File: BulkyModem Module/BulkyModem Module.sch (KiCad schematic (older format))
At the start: 13 parts, among them M1 Mounting, M2 Mounting, M3 Mounting, M4 Mounting, U1 74HCT244, U6 74HCT32

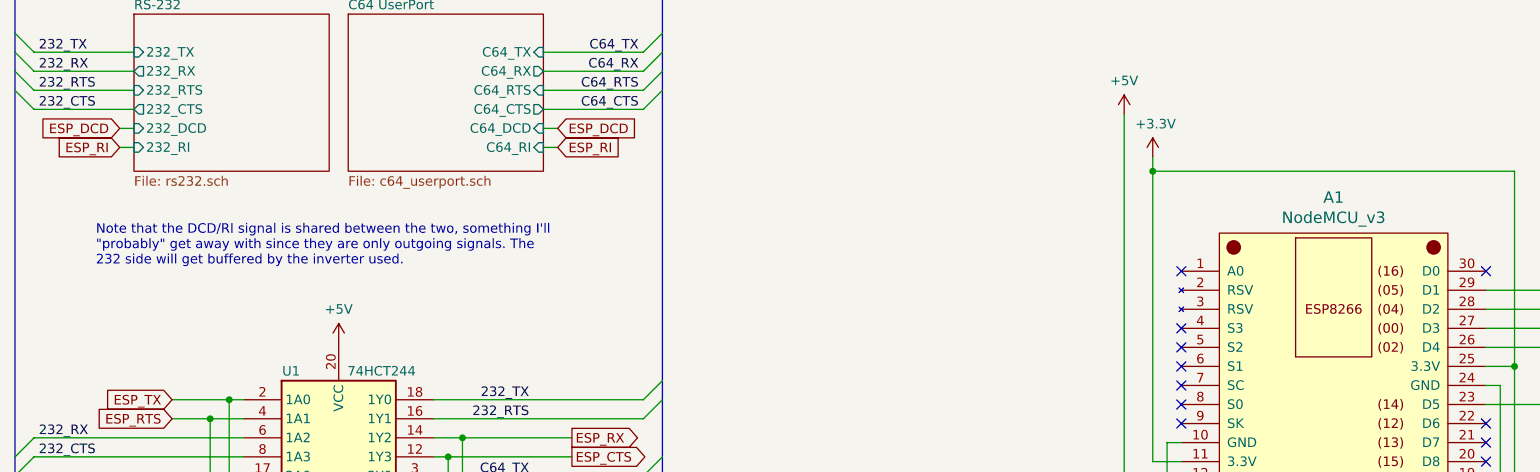
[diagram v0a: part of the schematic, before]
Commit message: Updated UserPort layout
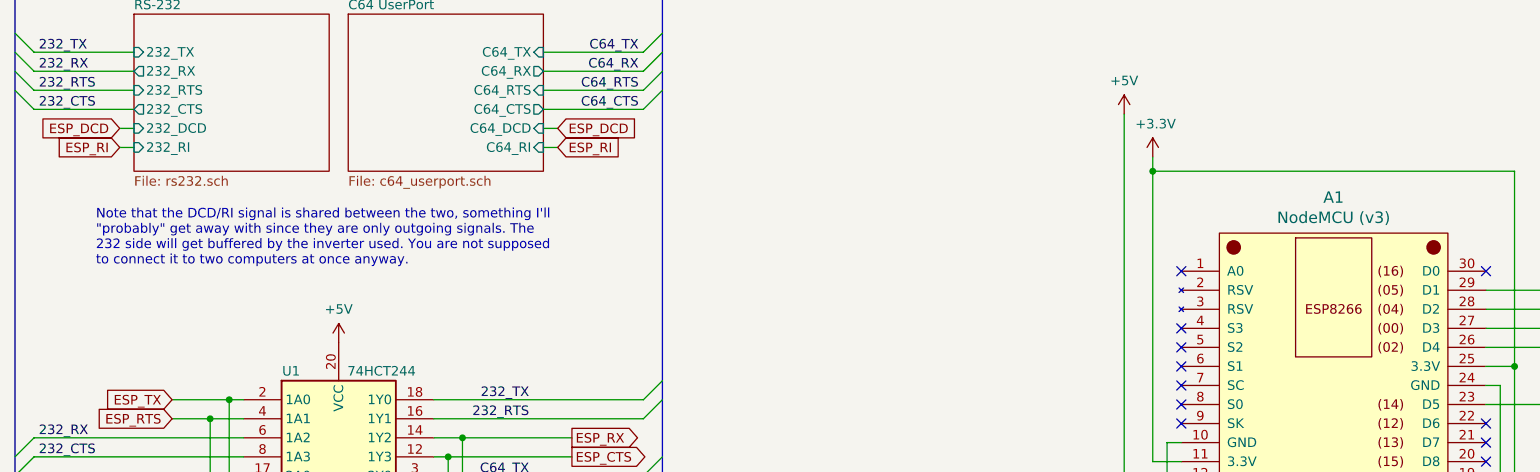
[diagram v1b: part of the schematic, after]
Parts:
- A1: value NodeMCU_v3 -> NodeMCU (v3)
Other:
- note added: "Note that the DCD/RI signal is shared between the two, something I'll\n"probably" get away with since they are only outgoing signals. The\n232 side will get buffered by the inverter used. You are not supposed\nto connect it to two computers at once anyway."
- note removed: "Note that the DCD/RI signal is shared between the two, something I'll\n"probably" get away with since they are only outgoing signals. The\n232 side will get buffered by the inverter used."
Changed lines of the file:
@@
 P 7650 3625
 F 0 "A1" H 7650 4712 60  0000 C CNN
-F 1 "NodeMCU_v3" H 7650 4606 60  0000 C CNN
+F 1 "NodeMCU (v3)" H 7650 4606 60  0000 C CNN
 F 2 "nodemcu_v3:NodeMCU-LoLinV3" H 7050 2775 60  0001 C CNN
 F 3 "" H 7050 2775 60  0000 C CNN
@@
 	3575 2175 3500 2175
 Text Notes 1150 2900 0    50   ~ 0
-Note that the DCD/RI signal is shared between the two, something I'll\n"probably" get away with since they are only outgoing signals. The\n232 side will get buffered by the inverter used.
+Note that the DCD/RI signal is shared between the two, something I'll\n"probably" get away with since they are only outgoing signals. The\n232 side will get buffered by the inverter used. You are not supposed\nto connect it to two computers at once anyway.
 Text GLabel 1275 2275 0    50   Input ~ 0
 ESP_RI

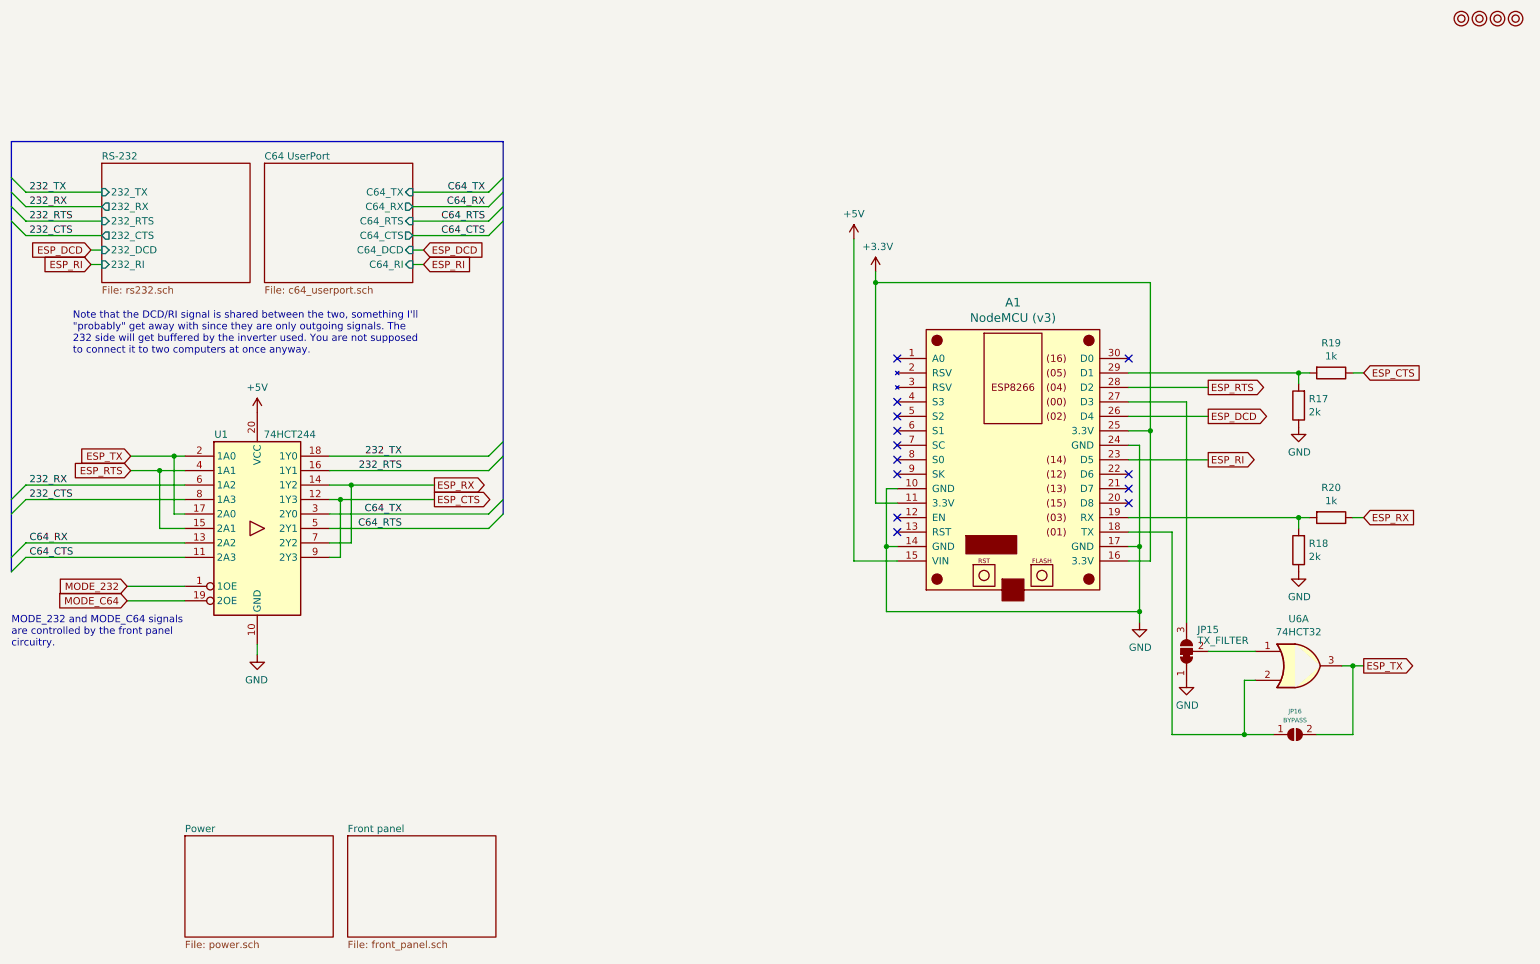
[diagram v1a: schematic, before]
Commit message: Revised version. Mainly buffering signals
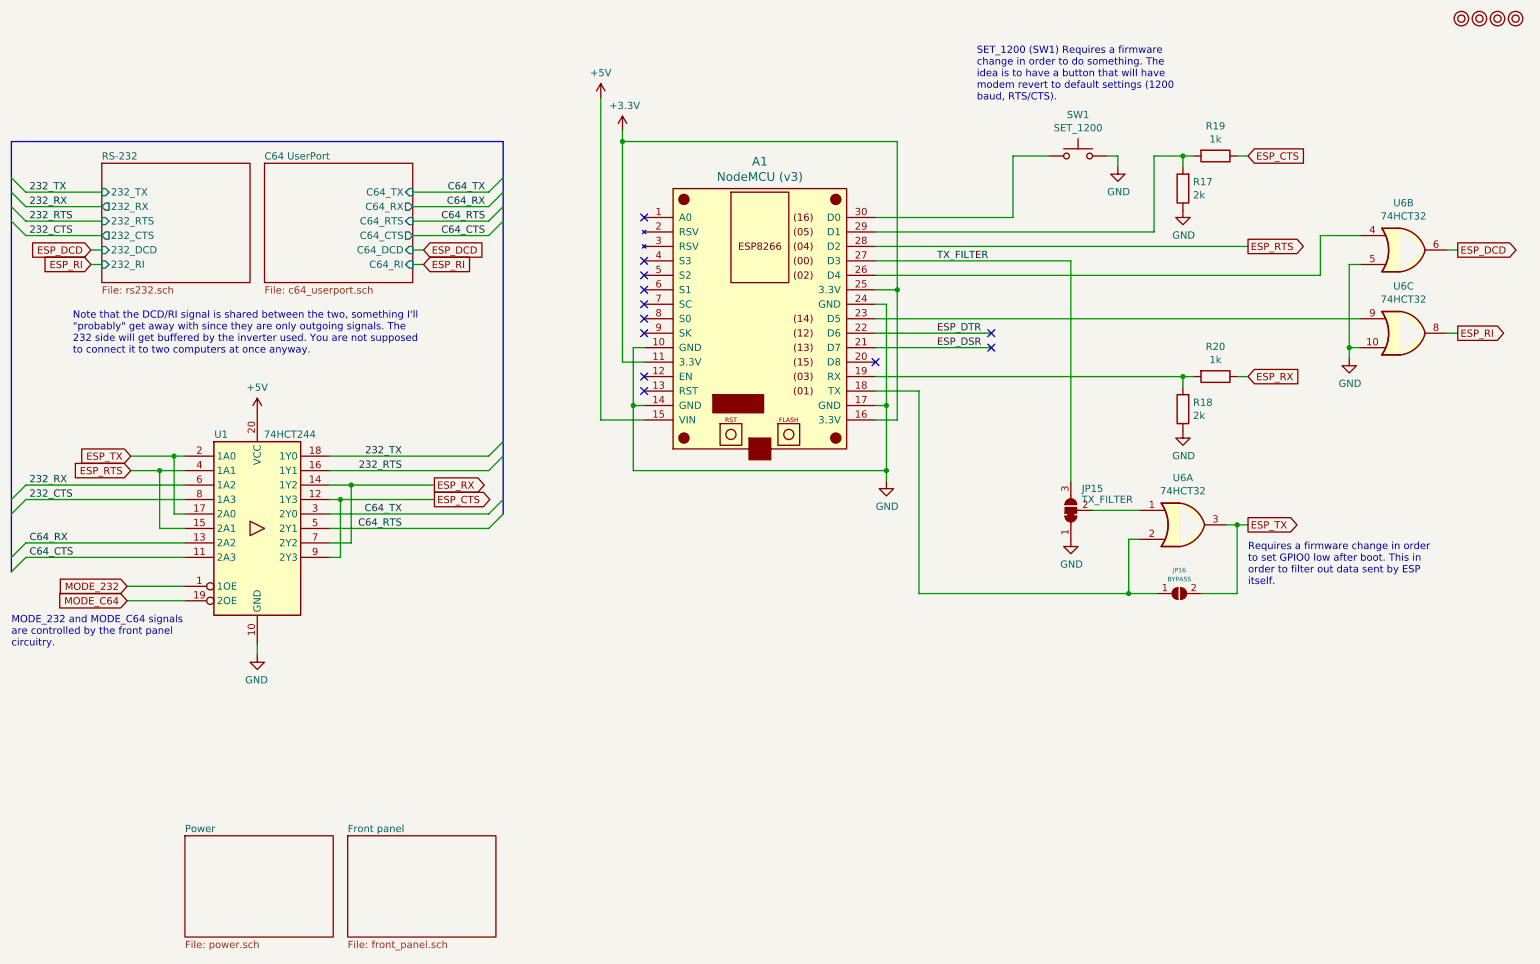
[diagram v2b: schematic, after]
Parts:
- added SW1: SET_1200, Button_Switch_THT:SW_Tactile_SPST_Angled_PTS645Vx39-2LFS, symbol Switch:SW_Push
- added unit 2 of U6
- added unit 3 of U6
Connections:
- net ESP_DCD: now also U6.6; no longer A1.26 (D4)
- net ESP_RI: now also U6.8; no longer A1.23 (D5)
- net GND: now also SW1.2, U6.10, U6.5
- net ESP_DSR: now reaches A1.21 (D7)
- net ESP_DTR: now reaches A1.22 (D6)
- net TX_FILTER: now reaches A1.27 (D3), JP15.3 (B)
- net at A1.30 (D0): now also SW1.1
- new net: A1.23 (D5), U6.9
- new net: A1.26 (D4), U6.4
- no-connect marks 13 -> 12
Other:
- note added: "Requires a firmware change in order\nto set GPIO0 low after boot. This in\norder to filter out data sent by ESP\nitself."
- note added: "SET_1200 (SW1) Requires a firmware\nchange in order to do something. The\nidea is to have a button that will have\nmodem revert to default settings (1200\nbaud, RTS/CTS)."
- moved on the sheet: A1, JP15, JP16, R17, R18, R19, R20, U6A

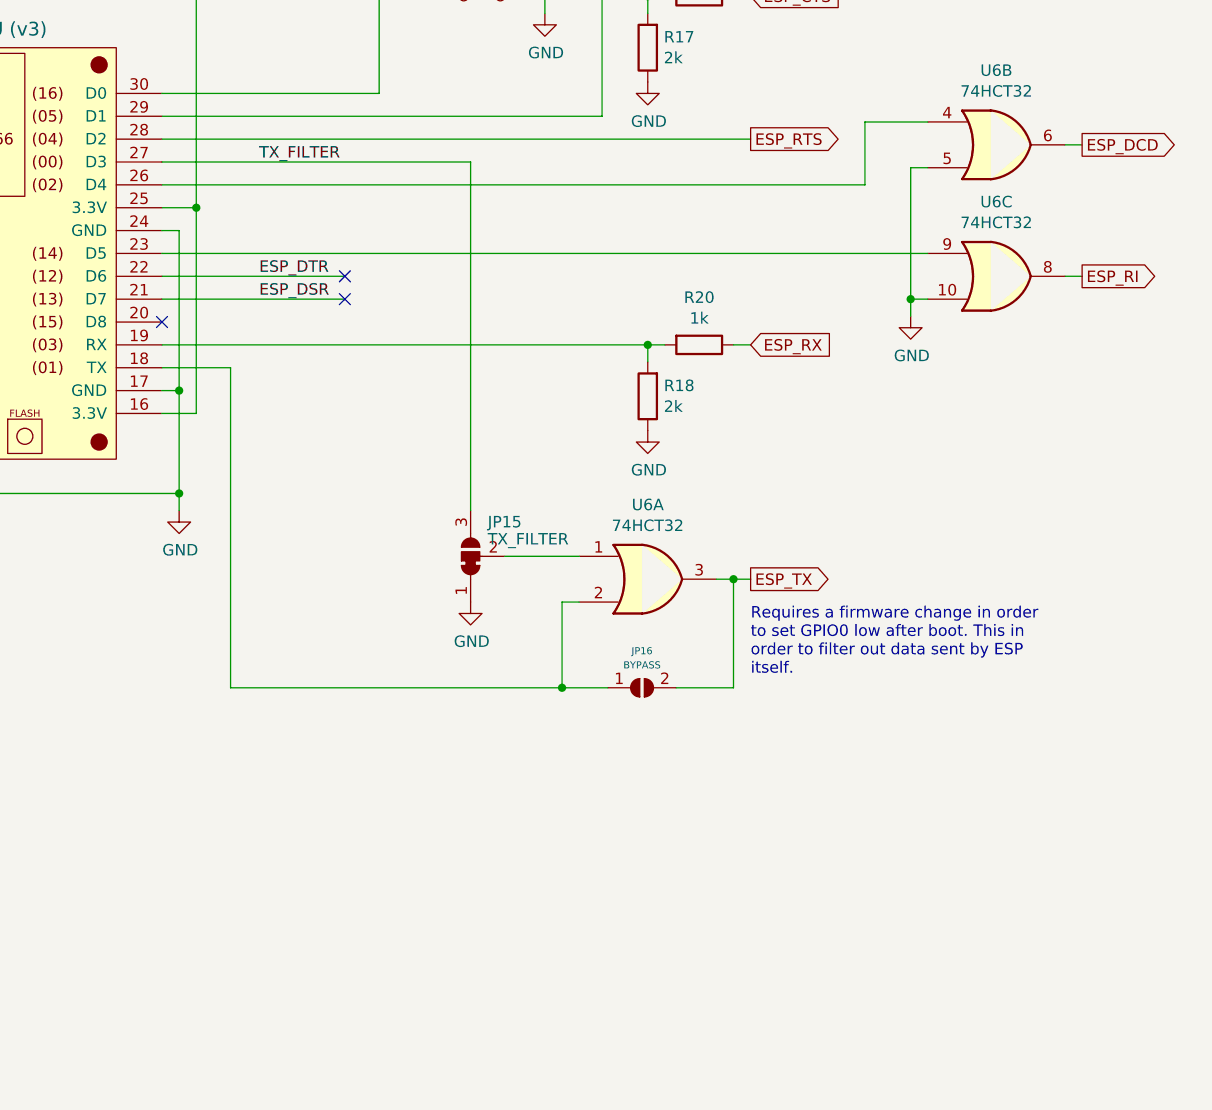
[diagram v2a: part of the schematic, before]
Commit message: Tweaks needed to make revision C actually work.
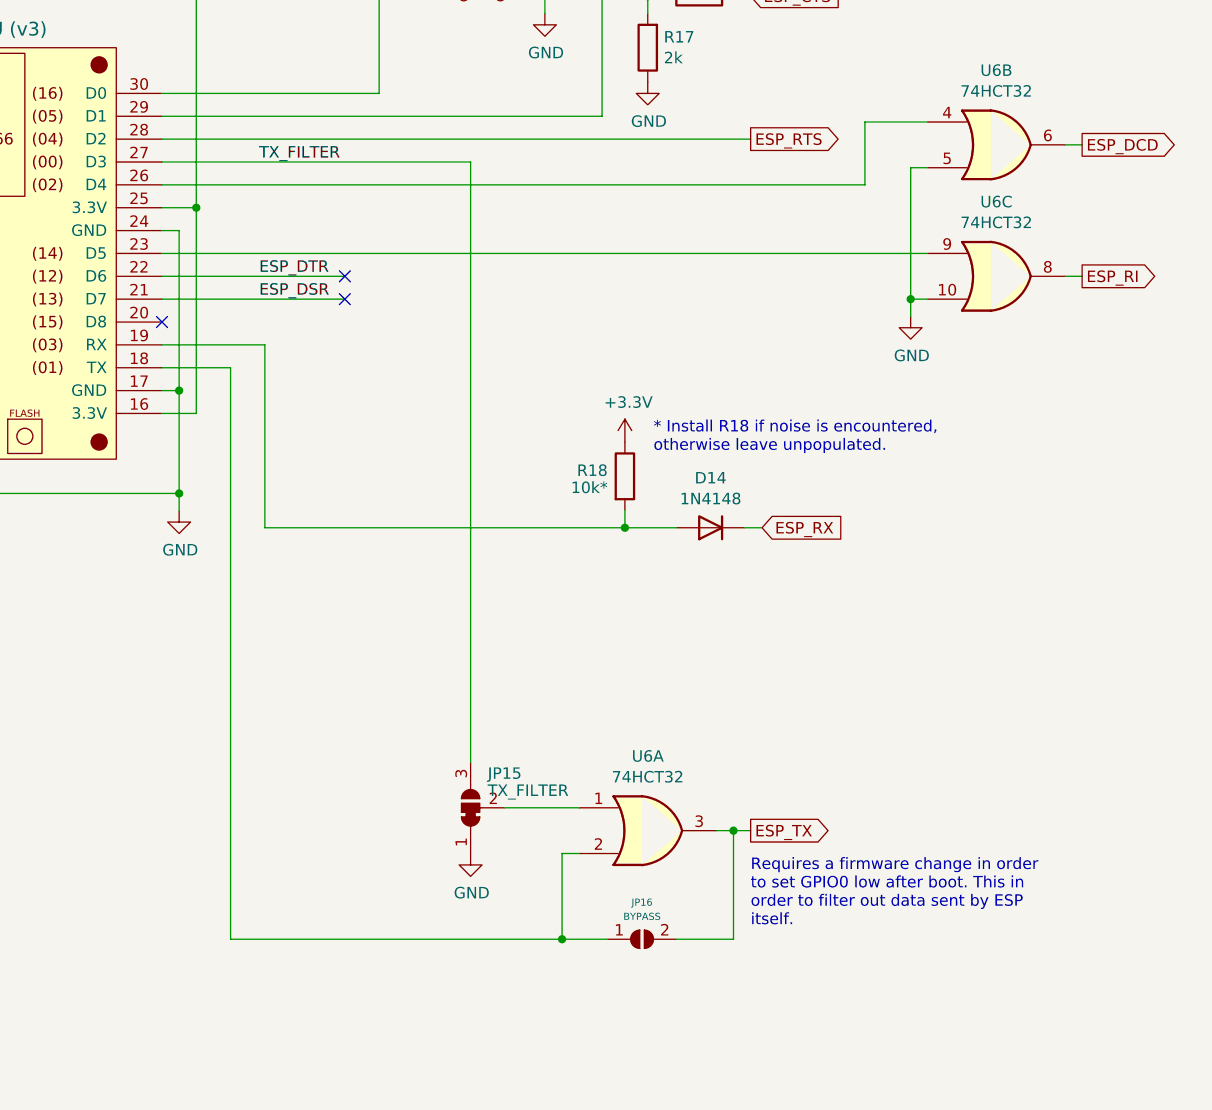
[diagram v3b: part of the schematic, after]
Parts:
- removed R20: 1k, resistor:R_Axial_DIN0207_L6.3mm_D2.5mm_P10.16mm_Horizontal, symbol Device:R
- added D14: 1N4148, Diode_THT:D_DO-35_SOD27_P7.62mm_Horizontal, symbol Diode:1N4148
- R18: value 2k -> 10k*
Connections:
- net +3V3: now also R18.1
- net ESP_RX: now also D14.1 (K)
- net GND: no longer R18.1
- net at A1.19 (RX), R18.2: now also D14.2 (A)
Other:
- note added: "* Install R18 if noise is encountered,\notherwise leave unpopulated."
- moved on the sheet: JP15, JP16, R18, U6A
